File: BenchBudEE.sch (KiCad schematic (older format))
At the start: 0 parts

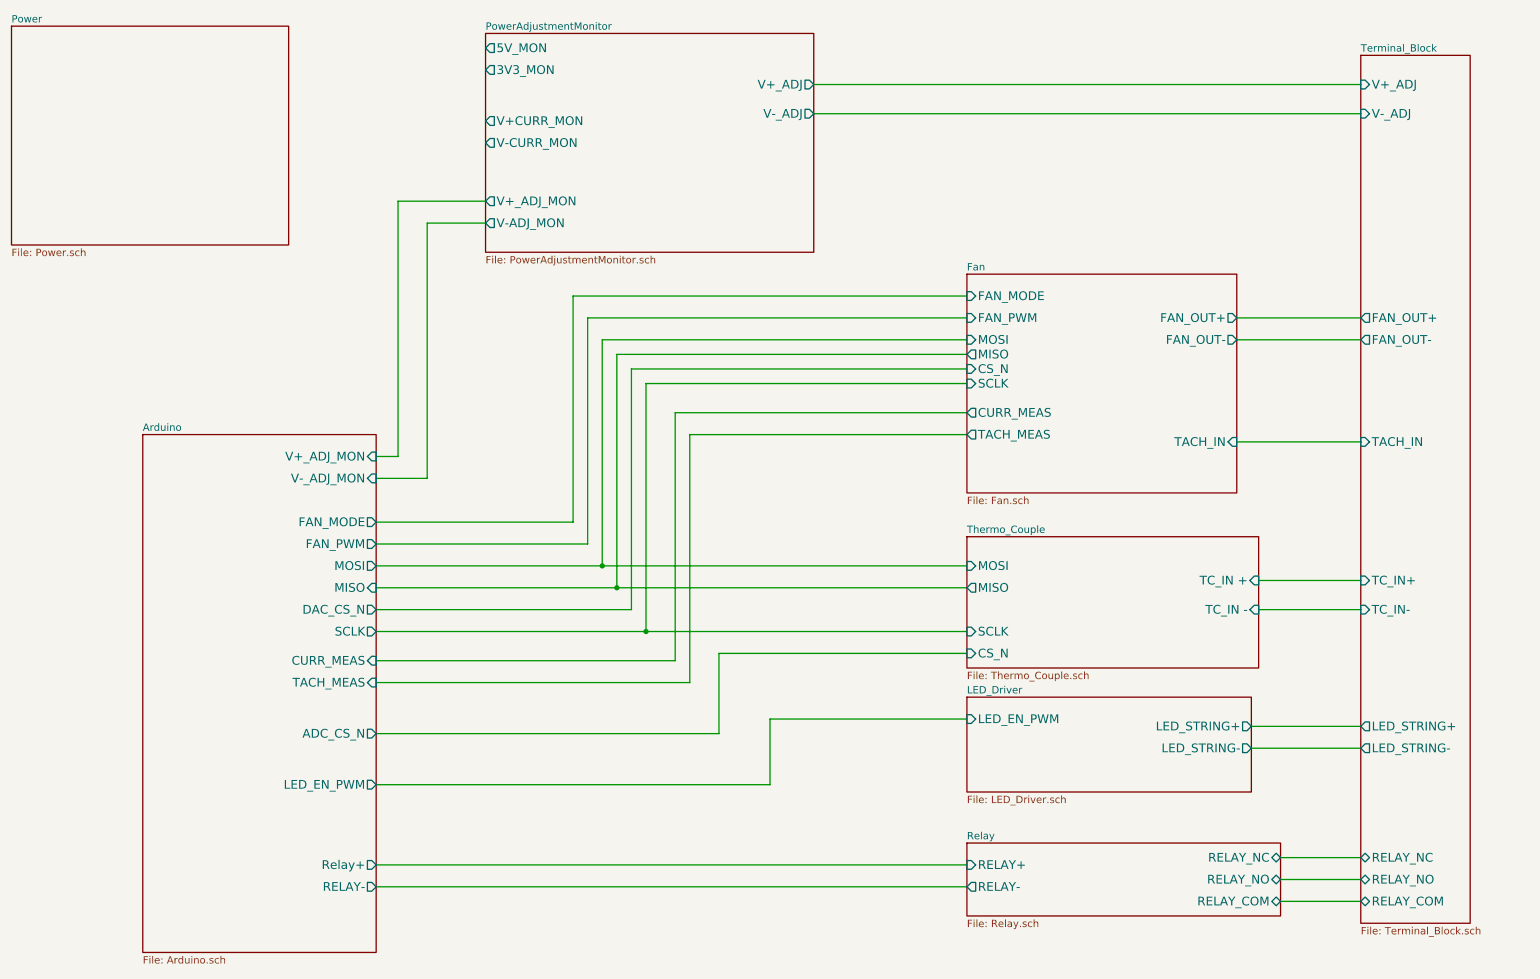
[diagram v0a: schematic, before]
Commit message: Added Arduino Connect Pin Layout
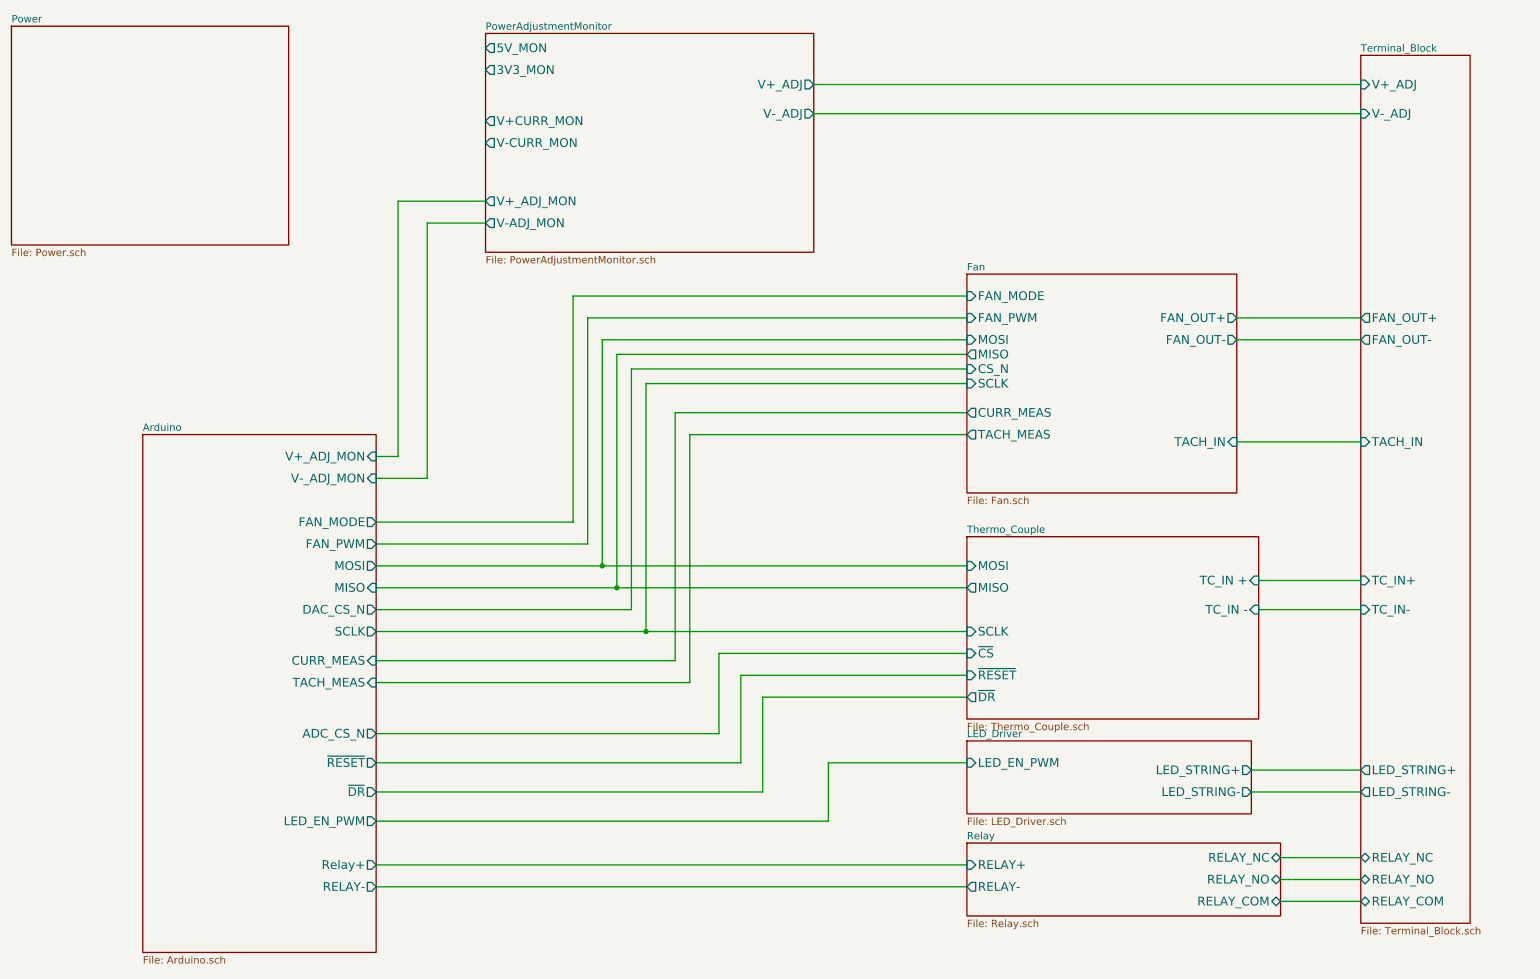
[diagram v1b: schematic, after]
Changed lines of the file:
@@
 F9 "V+_ADJ_MON" I R 3250 3700 60
 F10 "V-_ADJ_MON" I R 3250 3850 60
-F11 "LED_EN_PWM" O R 3250 5950 60
+F11 "LED_EN_PWM" O R 3250 6200 60
 F12 "DAC_CS_N" O R 3250 4750 60
 F13 "ADC_CS_N" O R 3250 5600 60
 F14 "FAN_PWM" O R 3250 4300 60
 F15 "FAN_MODE" O R 3250 4150 60
+F16 "~RESET" O R 3250 5800 60
+F17 "~DR" O R 3250 6000 60
 $EndSheet
 $Sheet
@@
 $EndSheet
 $Sheet
-S 7300 5350 1950 650
+S 7300 5650 1950 500
 U 52EECDCB
 F0 "LED_Driver" 50
 F1 "LED_Driver.sch" 50
-F2 "LED_EN_PWM" I L 7300 5500 60
-F3 "LED_STRING+" O R 9250 5550 60
-F4 "LED_STRING-" O R 9250 5700 60
+F2 "LED_EN_PWM" I L 7300 5800 60
+F3 "LED_STRING+" O R 9250 5850 60
+F4 "LED_STRING-" O R 9250 6000 60
 $EndSheet
 $Sheet
@@
 	3600 2100 4000 2100
 $Sheet
-S 7300 4250 2000 900
+S 7300 4250 2000 1250
 U 52EECD62
 F0 "Thermo_Couple" 50
@@
 F2 "MISO" O L 7300 4600 60
 F3 "SCLK" I L 7300 4900 60
-F4 "CS_N" I L 7300 5050 60
-F5 "MOSI" I L 7300 4450 60
-F6 "TC_IN +" I R 9300 4550 60
-F7 "TC_IN -" I R 9300 4750 60
+F4 "MOSI" I L 7300 4450 60
+F5 "TC_IN +" I R 9300 4550 60
+F6 "TC_IN -" I R 9300 4750 60
+F7 "~CS" I L 7300 5050 60
+F8 "~RESET" I L 7300 5200 60
+F9 "~DR" O L 7300 5350 60
 $EndSheet
 $Sheet
@@
 F5 "FAN_OUT-" O L 10000 2900 60
 F6 "TACH_IN" I L 10000 3600 60
-F7 "LED_STRING+" O L 10000 5550 60
-F8 "LED_STRING-" O L 10000 5700 60
+F7 "LED_STRING+" O L 10000 5850 60
+F8 "LED_STRING-" O L 10000 6000 60
 F9 "TC_IN+" I L 10000 4550 60
 F10 "TC_IN-" I L 10000 4750 60
@@
 	5600 5050 7300 5050
 Wire Wire Line
-	7300 5500 5950 5500
-Wire Wire Line
-	5950 5500 5950 5950
-Wire Wire Line
-	5950 5950 3250 5950
+	7300 5800 6350 5800
+Wire Wire Line
+	6350 5800 6350 6200
+Wire Wire Line
+	6350 6200 3250 6200
 Wire Wire Line
 	3250 6500 7300 6500
@@
 	9150 2750 10000 2750
 Wire Wire Line
-	9250 5550 10000 5550
-Wire Wire Line
-	9250 5700 10000 5700
+	9250 6000 10000 6000
+Wire Wire Line
+	9250 5850 10000 5850
 Wire Wire Line
 	3250 4150 4600 4150
@@
 Wire Wire Line
 	4600 2600 7300 2600
+Wire Wire Line
+	3250 5800 5750 5800
+Wire Wire Line
+	5750 5800 5750 5200
+Wire Wire Line
+	5750 5200 7300 5200
+Wire Wire Line
+	7300 5350 5900 5350
+Wire Wire Line
+	5900 5350 5900 6000
+Wire Wire Line
+	5900 6000 3250 6000
 $EndSCHEMATC

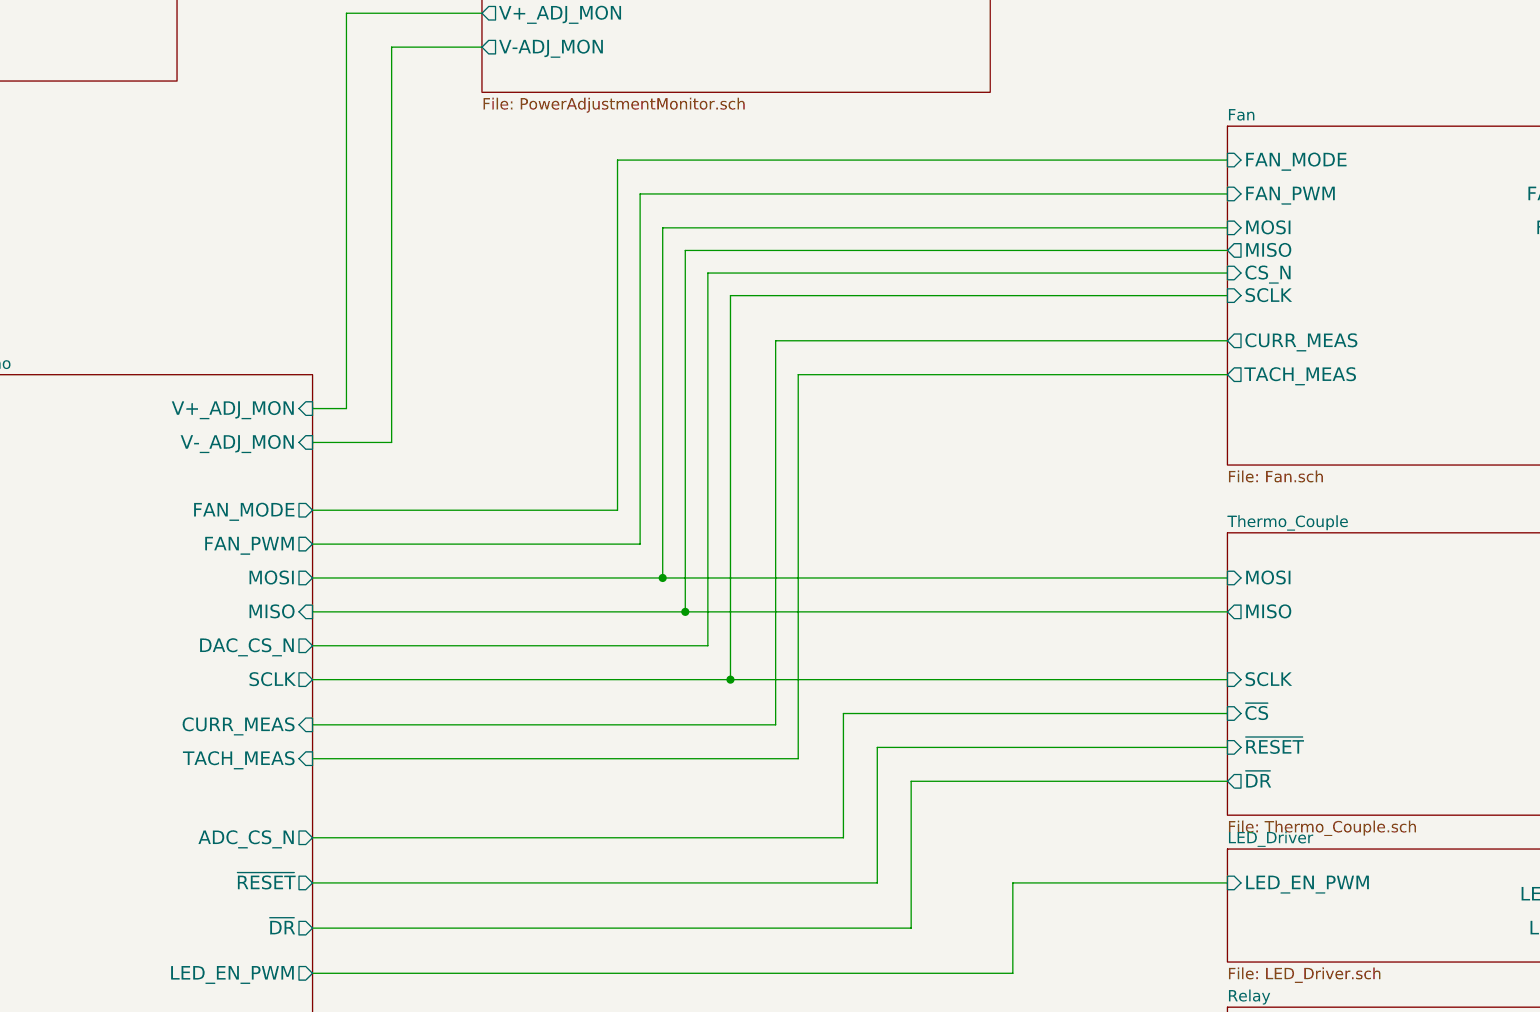
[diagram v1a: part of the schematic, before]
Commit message: Associate and Place Power Component
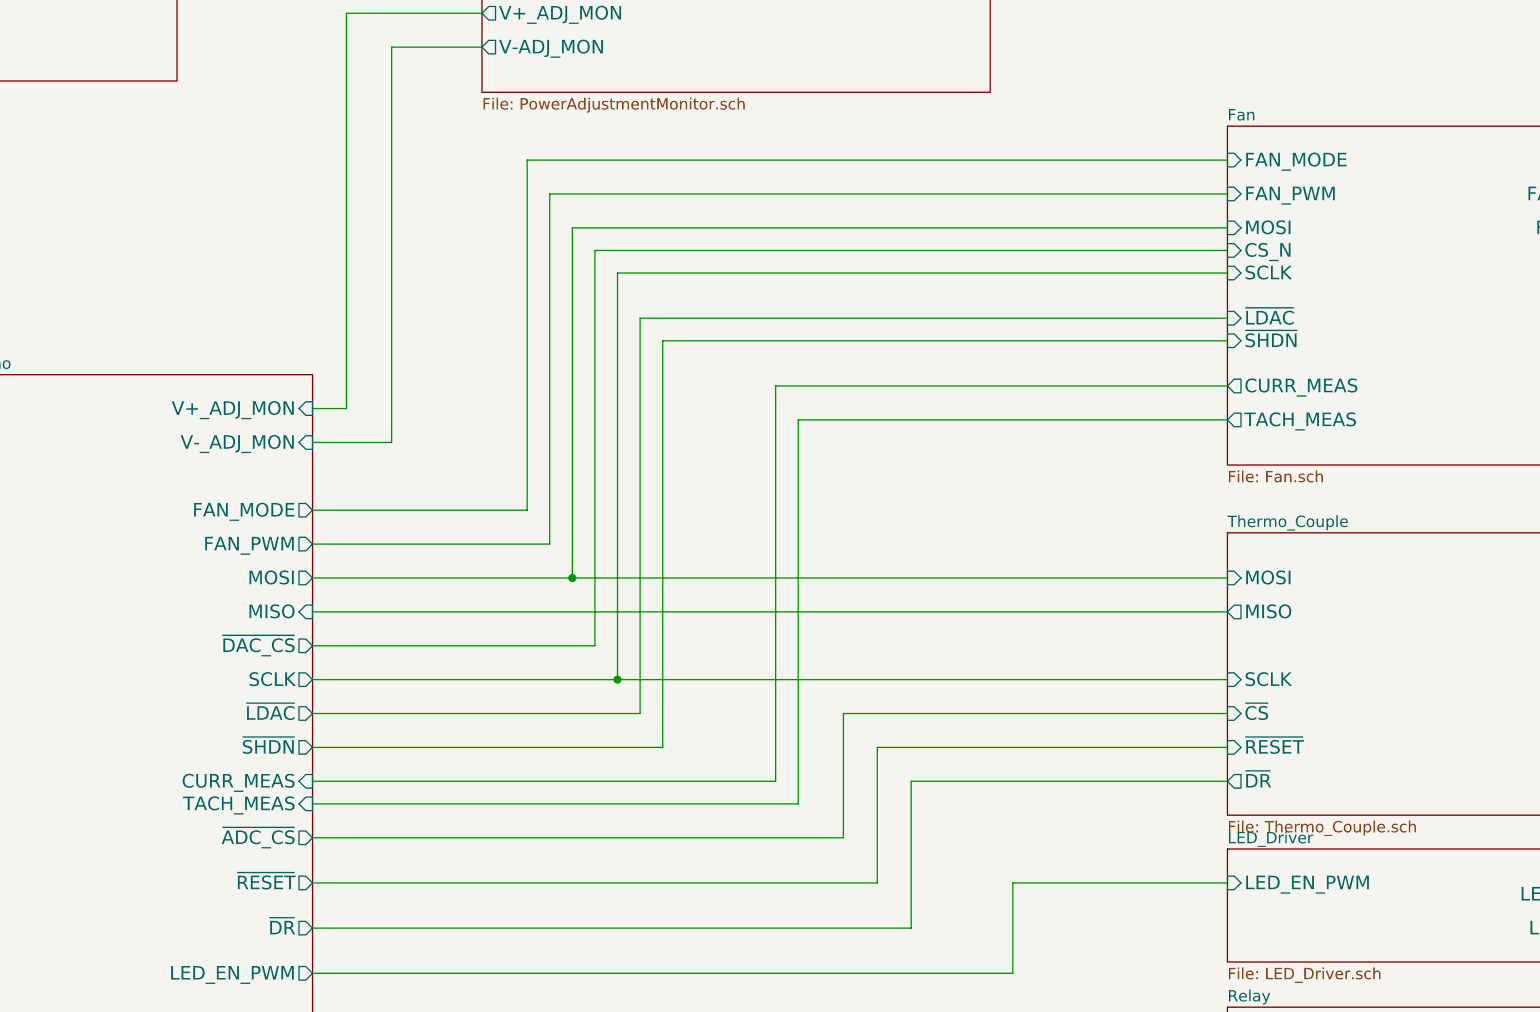
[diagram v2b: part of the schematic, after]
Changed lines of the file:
@@
 Sheet 1 9
 Title ""
-Date "17 feb 2014"
+Date "23 feb 2014"
 Rev ""
 Comp ""
@@
 F4 "MISO" I R 3250 4600 60
 F5 "SCLK" O R 3250 4900 60
-F6 "TACH_MEAS" I R 3250 5250 60
+F6 "TACH_MEAS" I R 3250 5450 60
 F7 "RELAY-" O R 3250 6650 60
-F8 "CURR_MEAS" I R 3250 5100 60
+F8 "CURR_MEAS" I R 3250 5350 60
 F9 "V+_ADJ_MON" I R 3250 3700 60
 F10 "V-_ADJ_MON" I R 3250 3850 60
 F11 "LED_EN_PWM" O R 3250 6200 60
-F12 "DAC_CS_N" O R 3250 4750 60
-F13 "ADC_CS_N" O R 3250 5600 60
-F14 "FAN_PWM" O R 3250 4300 60
-F15 "FAN_MODE" O R 3250 4150 60
-F16 "~RESET" O R 3250 5800 60
-F17 "~DR" O R 3250 6000 60
+F12 "FAN_PWM" O R 3250 4300 60
+F13 "FAN_MODE" O R 3250 4150 60
+F14 "~RESET" O R 3250 5800 60
+F15 "~DR" O R 3250 6000 60
+F16 "~LDAC" O R 3250 5050 60
+F17 "~SHDN" O R 3250 5200 60
+F18 "~DAC_CS" O R 3250 4750 60
+F19 "~ADC_CS" O R 3250 5600 60
 $EndSheet
 $Sheet
@@
 F1 "Fan.sch" 50
 F2 "MOSI" I L 7300 2900 60
-F3 "MISO" O L 7300 3000 60
-F4 "CS_N" I L 7300 3100 60
-F5 "SCLK" I L 7300 3200 60
-F6 "FAN_OUT+" O R 9150 2750 60
-F7 "TACH_IN" I R 9150 3600 60
-F8 "TACH_MEAS" O L 7300 3550 60
-F9 "CURR_MEAS" O L 7300 3400 60
-F10 "FAN_OUT-" O R 9150 2900 60
-F11 "FAN_PWM" I L 7300 2750 60
-F12 "FAN_MODE" I L 7300 2600 60
+F3 "CS_N" I L 7300 3000 60
+F4 "SCLK" I L 7300 3100 60
+F5 "FAN_OUT+" O R 9150 2750 60
+F6 "TACH_IN" I R 9150 3600 60
+F7 "TACH_MEAS" O L 7300 3750 60
+F8 "CURR_MEAS" O L 7300 3600 60
+F9 "FAN_OUT-" O R 9150 2900 60
+F10 "FAN_PWM" I L 7300 2750 60
+F11 "FAN_MODE" I L 7300 2600 60
+F12 "~LDAC" I L 7300 3300 60
+F13 "~SHDN" I L 7300 3400 60
 $EndSheet
 $Sheet
@@
 $EndSheet
 Wire Wire Line
-	7300 2750 4700 2750
-Wire Wire Line
-	4700 2750 4700 4300
-Wire Wire Line
-	4700 4300 3250 4300
-Wire Wire Line
-	4800 2900 4800 4450
-Wire Wire Line
-	4800 2900 7300 2900
+	7300 2750 4300 2750
+Wire Wire Line
+	4300 2750 4300 4300
+Wire Wire Line
+	4300 4300 3250 4300
+Wire Wire Line
+	4400 2900 4400 4450
+Wire Wire Line
+	4400 2900 7300 2900
 Wire Wire Line
 	3250 4450 7300 4450
@@
 	3250 4600 7300 4600
 Wire Wire Line
-	4900 3000 4900 4600
-Wire Wire Line
-	4900 3000 7300 3000
-Wire Wire Line
-	5000 4750 3250 4750
-Wire Wire Line
-	5000 3100 5000 4750
-Wire Wire Line
-	5000 3100 7300 3100
-Wire Wire Line
-	7300 3200 5100 3200
-Wire Wire Line
-	5100 3200 5100 4900
+	4500 4750 3250 4750
+Wire Wire Line
+	4500 3000 4500 4750
+Wire Wire Line
+	4500 3000 7300 3000
+Wire Wire Line
+	7300 3100 4600 3100
+Wire Wire Line
+	4600 3100 4600 4900
 Wire Wire Line
 	3250 4900 7300 4900
 Wire Wire Line
-	5300 5100 3250 5100
-Wire Wire Line
-	5300 3400 5300 5100
-Wire Wire Line
-	5300 3400 7300 3400
-Wire Wire Line
-	7300 3550 5400 3550
-Wire Wire Line
-	5400 3550 5400 5250
-Wire Wire Line
-	5400 5250 3250 5250
-Connection ~ 4800 4450
-Connection ~ 4900 4600
-Connection ~ 5100 4900
+	5300 5350 3250 5350
+Wire Wire Line
+	5300 3600 5300 5350
+Wire Wire Line
+	5300 3600 7300 3600
+Wire Wire Line
+	7300 3750 5400 3750
+Wire Wire Line
+	5400 3750 5400 5450
+Wire Wire Line
+	5400 5450 3250 5450
+Connection ~ 4400 4450
+Connection ~ 4600 4900
 Wire Wire Line
 	3250 5600 5600 5600
@@
 	9250 5850 10000 5850
 Wire Wire Line
-	3250 4150 4600 4150
-Wire Wire Line
-	4600 4150 4600 2600
-Wire Wire Line
-	4600 2600 7300 2600
+	3250 4150 4200 4150
+Wire Wire Line
+	4200 4150 4200 2600
+Wire Wire Line
+	4200 2600 7300 2600
 Wire Wire Line
 	3250 5800 5750 5800
@@
 Wire Wire Line
 	5900 6000 3250 6000
+Wire Wire Line
+	3250 5050 4700 5050
+Wire Wire Line
+	4700 5050 4700 3300
+Wire Wire Line
+	4700 3300 7300 3300
+Wire Wire Line
+	3250 5200 4800 5200
+Wire Wire Line
+	4800 5200 4800 3400
+Wire Wire Line
+	4800 3400 7300 3400
 $EndSCHEMATC
